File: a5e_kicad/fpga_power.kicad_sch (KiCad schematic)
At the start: 27 parts, among them U1 A5EB013B-B23B

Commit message: add vias to lppdr balls
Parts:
- renumbered C1002 to C101, C1005 to C102, C1001 to C103, C1003 to C104, C1004 to C105, C1013 to C106, C1014 to C107, C1011 to C108, C1012 to C109, C1007 to C110, C1008 to C111, C607 to C112, C602 to C113, C604 to C114, C606 to C115, FB604 to FB10, FB601 to FB7, FB602 to FB8, FB603 to FB9, R601 to R47, R1002 to R48, R1001 to R49, R1003 to R50, R1004 to R51, R1005 to R52, R1006 to R53, U1 to U7

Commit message: add routes for power supplies
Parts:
- removed R48, R50, R52: 0R, Resistor_SMD:R_0402_1005Metric, symbol Device:R
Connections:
- net 1V3 is gone; now on net 1V2: U7.CG31 (VCCIO_PIO_2A_T), U7.CL31 (VCCIO_PIO_2A_T), U7.CL37 (VCCIO_PIO_2A_B), U7.CT37 (VCCIO_PIO_2A_B)
- net vccio_6b is gone; now on net 3V3: C101.1, C103.1, R49.2, U7.CT26 (VCCIO_HVIO_6B), U7.CW26 (VCCIO_HVIO_6B)
- net vccio_6c is gone; now on net 3V3: C104.1, C105.1, R51.2, U7.AG29 (VCCIO_HVIO_6C), U7.AL29 (VCCIO_HVIO_6C)
- net vccio_6x is gone; now on net 3V3: C106.1, C107.1, C108.1, C109.1, C110.1, C111.1, R53.2, U7.AW29 (VCCIO_HVIO_6D), U7.AW31 (VCCIO_HVIO_6D), U7.BF26 (VCCIO_HVIO_6H), U7.BJ26 (VCCIO_HVIO_6H), U7.BN26 (VCCIO_HVIO_6F), U7.BU26 (VCCIO_HVIO_6F), U7.CA29 (VCCIO_HVIO_6E), U7.CD29 (VCCIO_HVIO_6E), U7.CL29 (VCCIO_HVIO_6A), U7.CT29 (VCCIO_HVIO_6A)
- net 1V8: no longer U7.BJ29 (VCCIO_HVIO_6G), U7.BN29 (VCCIO_HVIO_6G)
- net 3V3: now also U7.BJ29 (VCCIO_HVIO_6G), U7.BN29 (VCCIO_HVIO_6G)

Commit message: savegame, after fixing wird problems with schematic sync
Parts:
- removed FB10, FB7, FB8, FB9: FerriteBead_Small, Capacitor_SMD:C_0603_1608Metric, symbol Device:FerriteBead_Small
- removed R47: 10K, Resistor_SMD:R_0402_1005Metric, symbol Device:R
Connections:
- net vccadc is gone; now on net 1V8: C112.1, U7.CG52 (VCCADC), U7.CL46 (VCCPLL_SDM)
- net vccplldighps is gone; now on net VCORE: C113.1, U7.BB52 (VCCPLLDIG2_HPS), U7.BB54 (VCCPLLDIG1_HPS)
- net vccplldigsdm is gone; now on net VCORE: C114.1, U7.CL49 (VCCPLLDIG_SDM)
- net vccpllhps is gone; now on net 1V8: C115.1, U7.BF52 (VCCPLL2_HPS), U7.BF57 (VCCPLL1_HPS)
- net 1v8: now reaches C102.1, U7.CG49 (VCCBAT)

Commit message: place even more bypass caps
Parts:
- removed R49, R51, R53: --, Resistor_SMD:R_0402_1005Metric, symbol Device:R

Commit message: route more rgmii io
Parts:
- C102: footprint Capacitor_SMD:C_0402_1005Metric -> Capacitor_SMD:C_0201_0603Metric
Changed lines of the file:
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@@
 			)
 		)
-		(property "Footprint" "Capacitor_SMD:C_0402_1005Metric"
+		(property "Footprint" "Capacitor_SMD:C_0201_0603Metric"
 			(at 44.1452 156.21 0)
 			(hide yes)

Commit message: lastest
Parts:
- removed C101, C104, C106, C108, C110: 100N, Capacitor_SMD:C_0402_1005Metric, symbol Device:C
- removed C103, C105, C107, C109, C111: 22U 6V3, Capacitor_SMD:C_0402_1005Metric, symbol Device:C
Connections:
- net 3V3 renamed 3v3

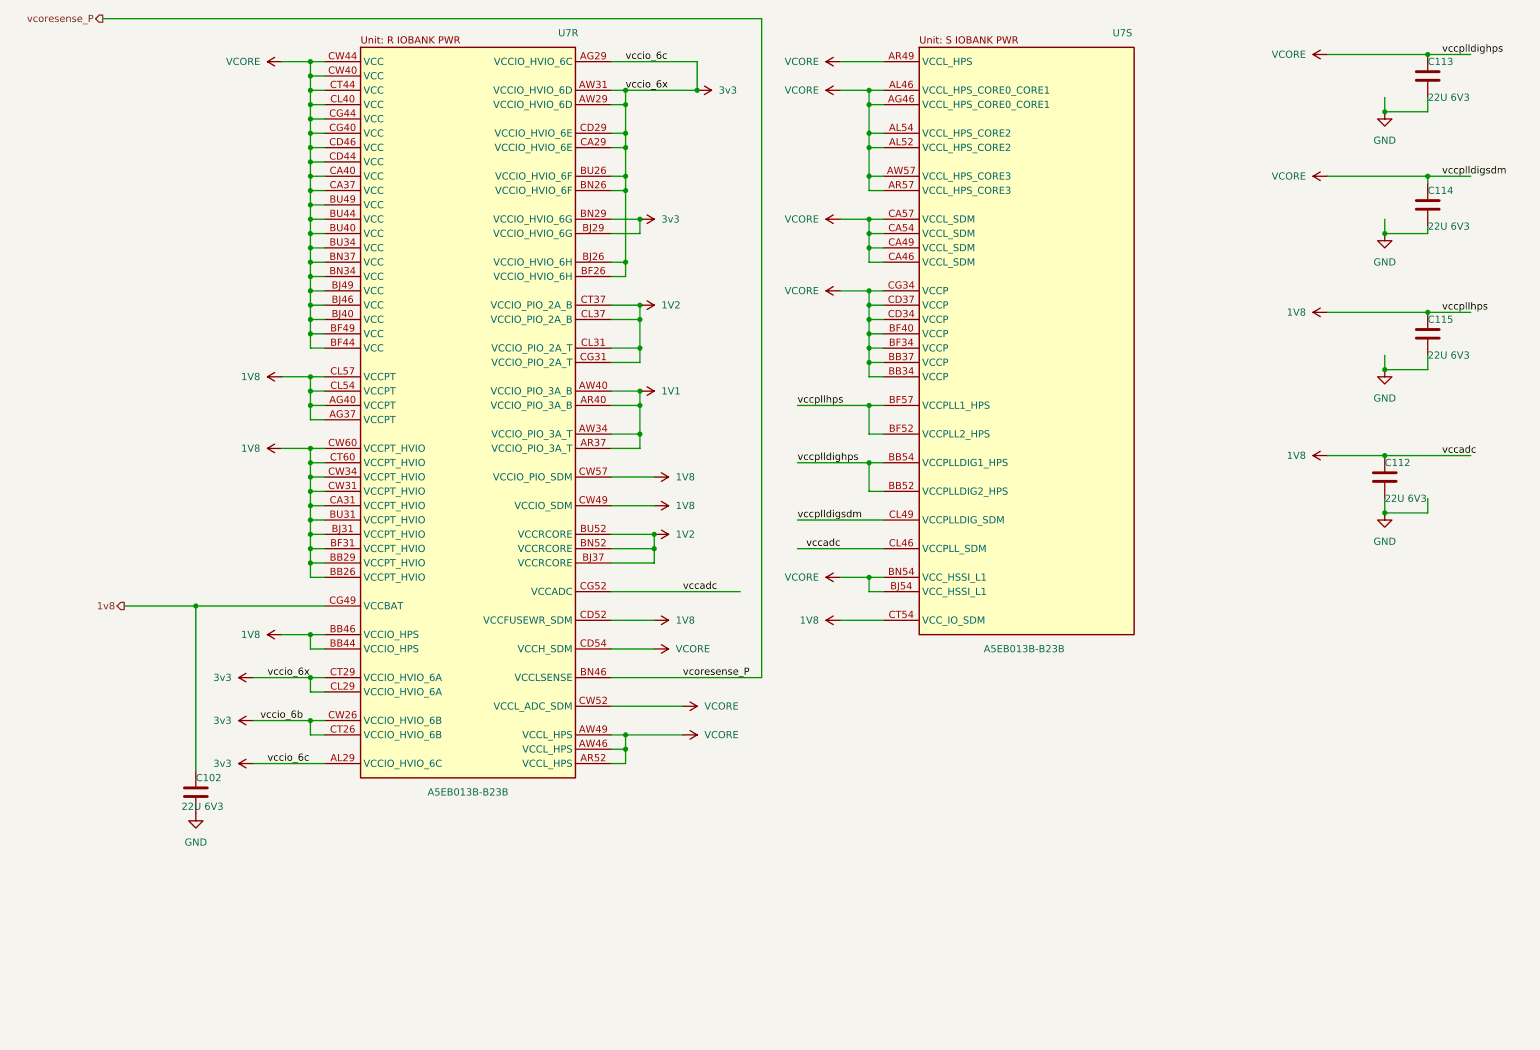
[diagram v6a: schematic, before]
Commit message: remove extra components and make 1v8 plane
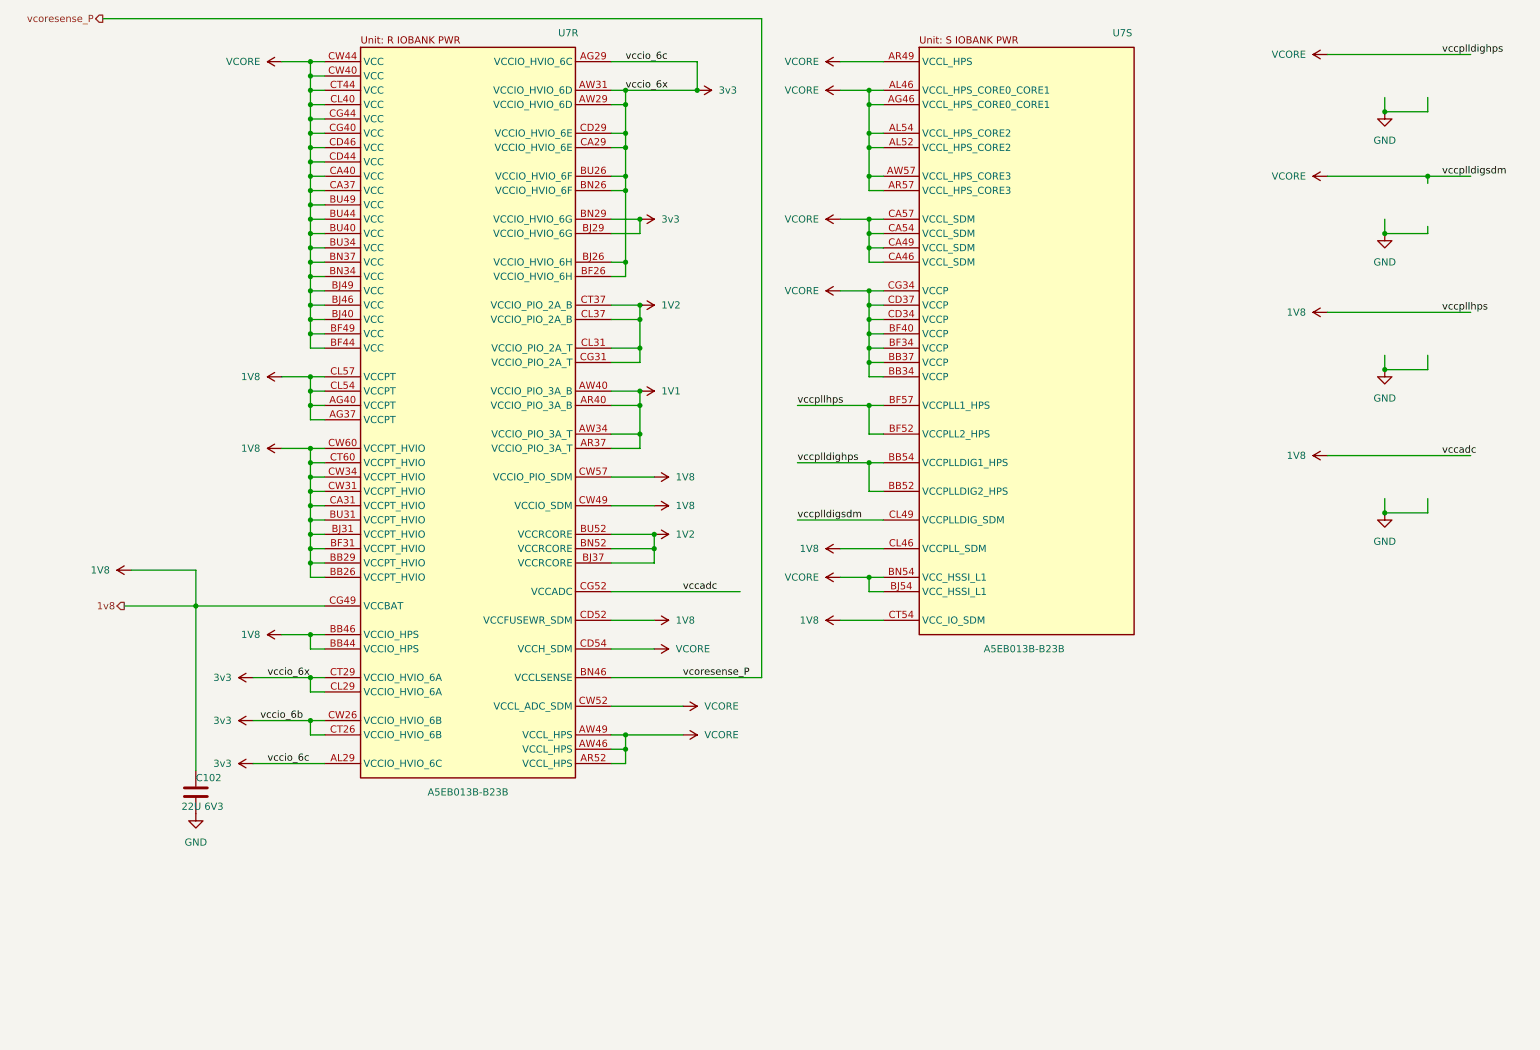
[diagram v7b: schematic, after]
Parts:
- removed C112, C113, C114, C115: 22U 6V3, Capacitor_SMD:C_0402_1005Metric, symbol Device:C
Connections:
- net 1v8 is gone; now on net 1V8: C102.1, U7.CG49 (VCCBAT)
